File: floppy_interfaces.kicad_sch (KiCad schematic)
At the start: 23 parts, among them J13 Conn_01x04_Male, J14 Conn_02x17_Odd_Even, J16 Conn_01x04_Male, J32 Mini-DIN-8-With-Shield, J6 SDF-60J for IEC 1541 serial p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, U1 74LS373, U2 74LVC374, U22 74LS06N, U3 74LVC374, U4 74LS373

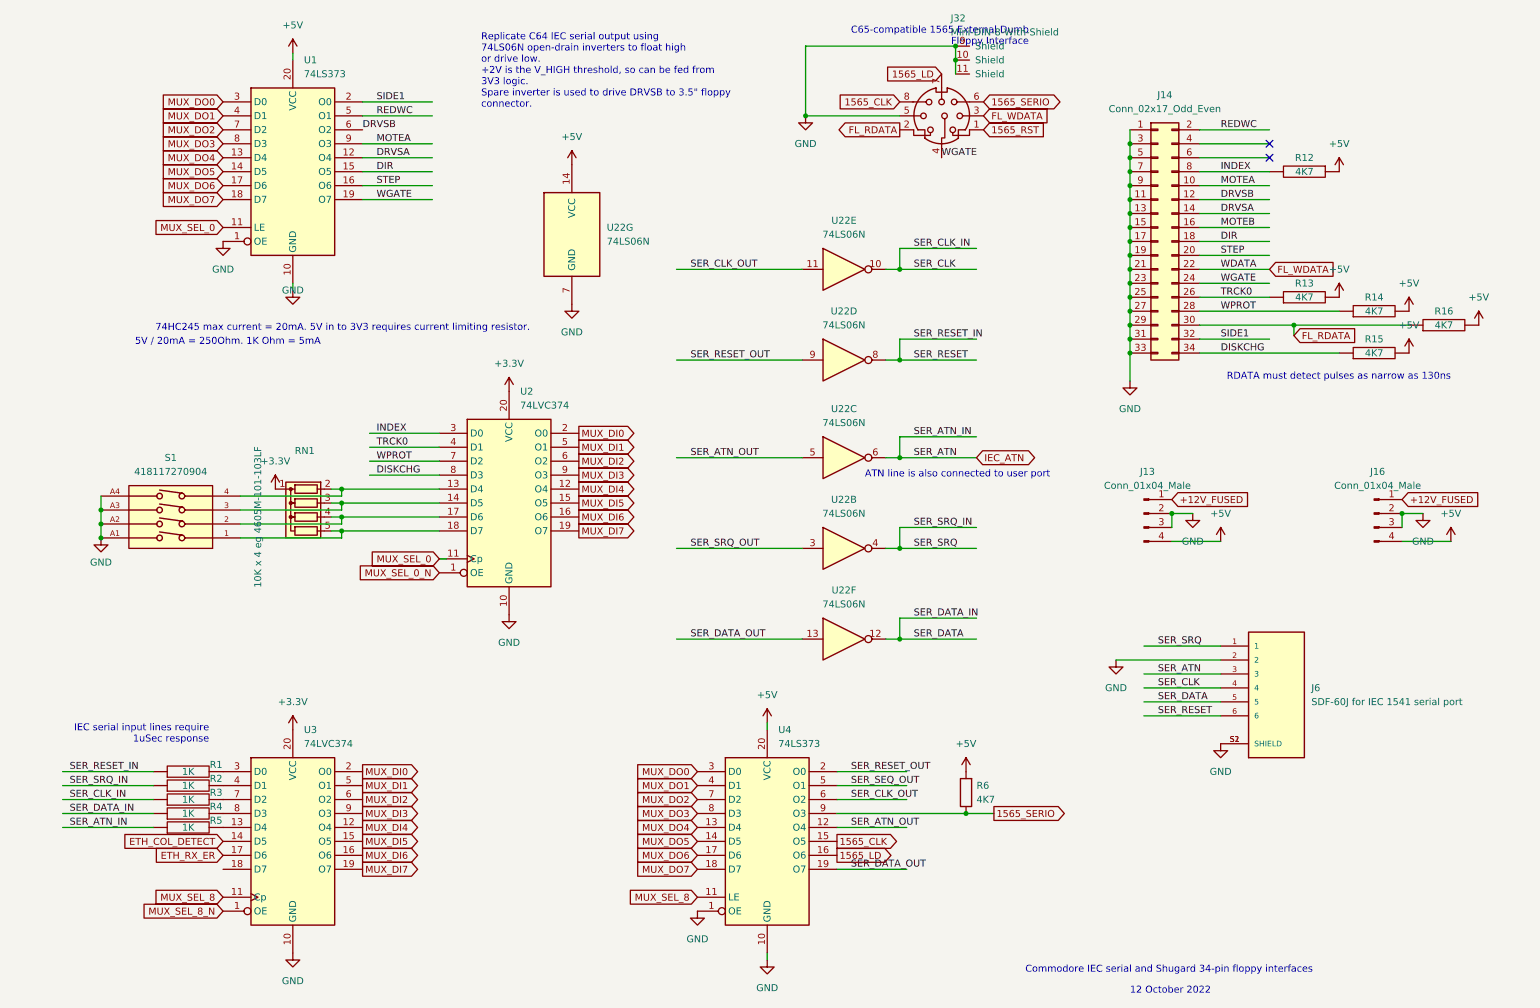
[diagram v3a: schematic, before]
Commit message: add footprints to differentiate 3.3V from 5V ICs
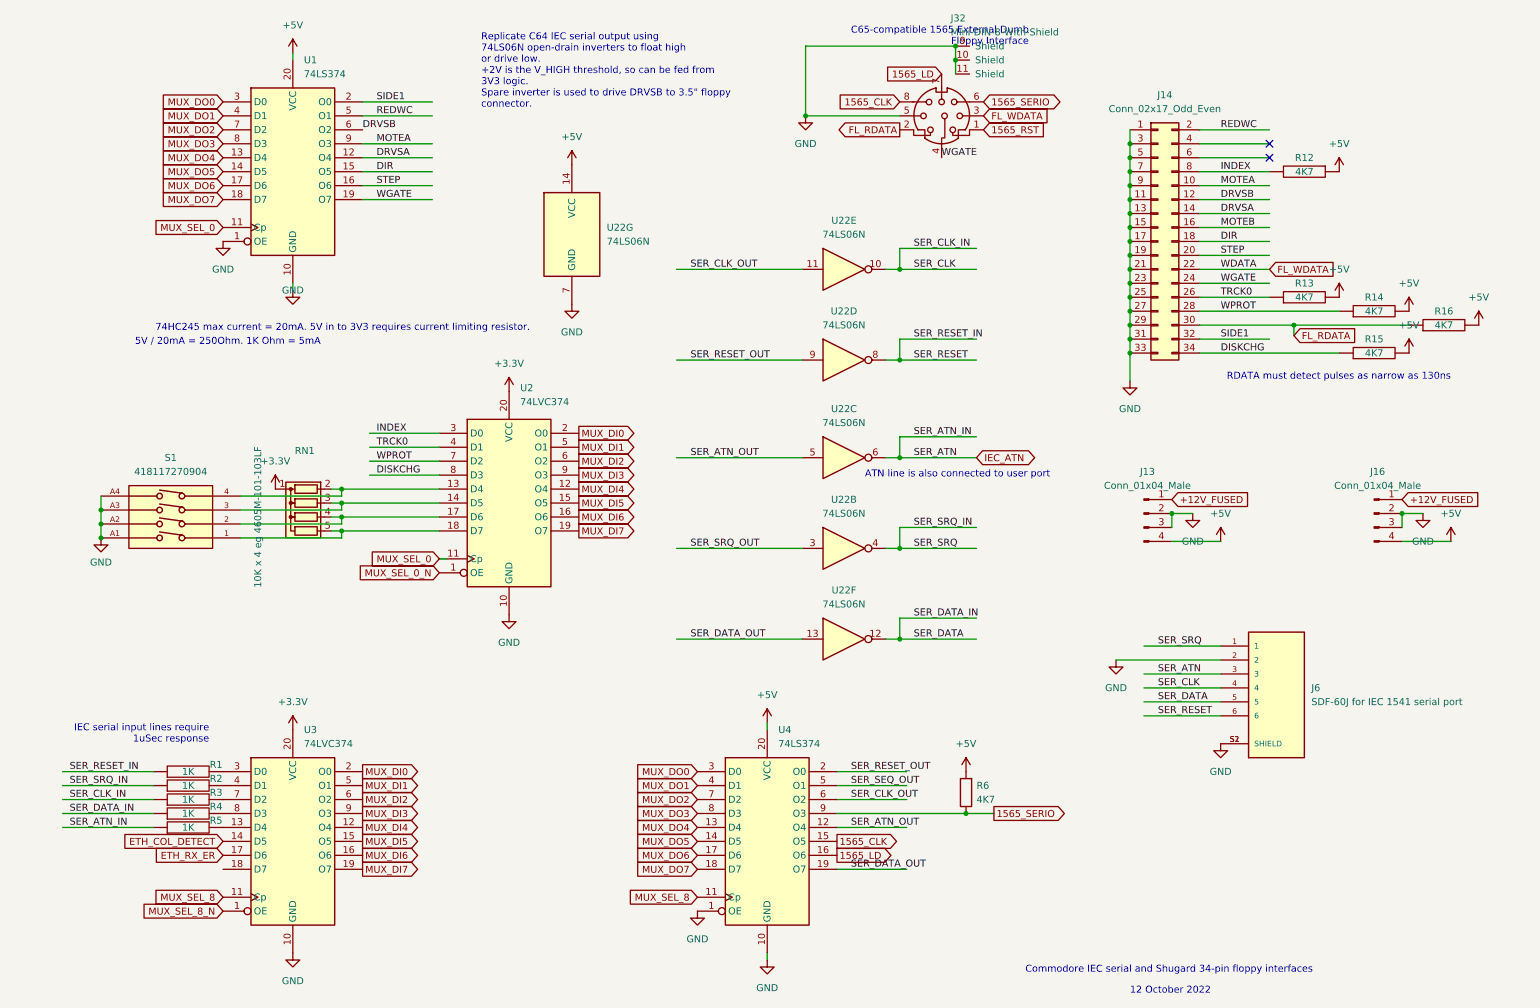
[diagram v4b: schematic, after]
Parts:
- removed U1, U4: 74LS373, Package_DIP:DIP-20_W7.62mm, symbol 74xx:74LS373
- added U1, U4: 74LS374, snapeda:DIP-20_LS_Family, symbol 74xx:74LS374
- U2, U3: footprint Package_DIP:DIP-20_W7.62mm -> snapeda:DIP-20_LVC_Family
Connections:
- net +5V: now also U1.20 (VCC), U4.20 (VCC)
- net 1565_CLK: now also U4.15 (O5)
- net 1565_LD: now also U4.16 (O6)
- net 1565_SERIO: now also U4.9 (O3)
- net DIR: now also U1.15 (O5)
- net DRVSA: now also U1.12 (O4)
- net DRVSB: now also U1.6 (O2)
- net GND: now also U1.1 (OE), U1.10 (GND), U4.1 (OE), U4.10 (GND)
- net MOTEA: now also U1.9 (O3)
- net MUX_DO0: now also U1.3 (D0), U4.3 (D0)
- net MUX_DO1: now also U1.4 (D1), U4.4 (D1)
- net MUX_DO2: now also U1.7 (D2), U4.7 (D2)
- net MUX_DO3: now also U1.8 (D3), U4.8 (D3)
- net MUX_DO4: now also U1.13 (D4), U4.13 (D4)
- net MUX_DO5: now also U1.14 (D5), U4.14 (D5)
- net MUX_DO6: now also U1.17 (D6), U4.17 (D6)
- net MUX_DO7: now also U1.18 (D7), U4.18 (D7)
- net MUX_SEL_0: now also U1.11 (Cp)
- net MUX_SEL_8: now also U4.11 (Cp)
- net REDWC: now also U1.5 (O1)
- net SER_ATN_OUT: now also U4.12 (O4)
- net SER_CLK_OUT: now also U4.6 (O2)
- net SER_DATA_OUT: now also U4.19 (O7)
- net SER_RESET_OUT: now also U4.2 (O0)
- net SER_SEQ_OUT: now also U4.5 (O1)
- net SIDE1: now also U1.2 (O0)
- net STEP: now also U1.16 (O6)
- net WGATE: now also U1.19 (O7)

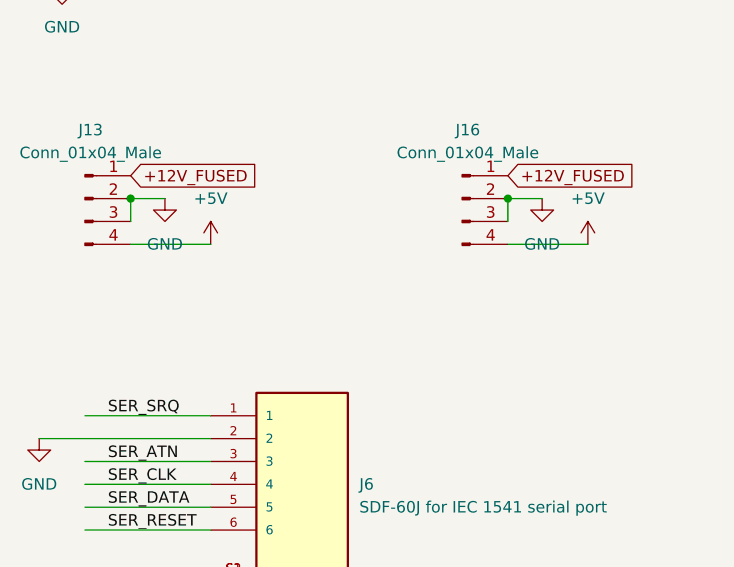
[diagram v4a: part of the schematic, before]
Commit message: fix many DRC warnings
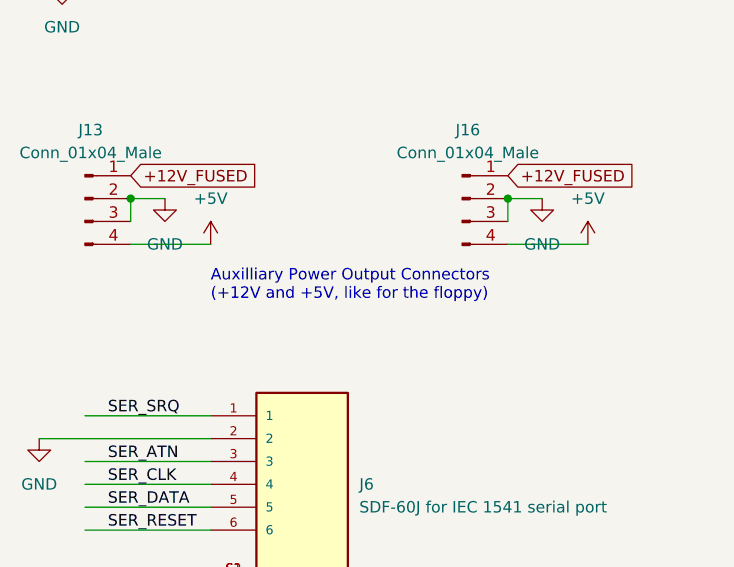
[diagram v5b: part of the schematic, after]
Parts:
- R1, R12, R13, R14, R15, R16, R2, R3, R4, R5: footprint Resistor_THT:R_Box_L8.4mm_W2.5mm_P5.08mm -> snapeda:Labeled Resistor
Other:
- note added: "Auxilliary Power Output Connectors (+12V and +5V, like for the floppy)"
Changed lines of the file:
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@@
     (effects (font (size 1.27 1.27)) (justify right bottom))
+  )
+  (text "Auxilliary Power Output Connectors\n(+12V and +5V, like for the floppy)"
+    (at 226.06 118.11 0)
+    (effects (font (size 1.27 1.27)) (justify left bottom))
   )
   (text "Replicate C64 IEC serial output using\n74LS06N open-drain inverters to float high\nor drive low.  \n+2V is the V_HIGH threshold, so can be fed from\n3V3 logic.\nSpare inverter is used to drive DRVSB to 3.5\" floppy\nconnector."
@@
     (property "Reference" "R13" (id 0) (at 241.3 64.77 90))
     (property "Value" "4K7" (id 1) (at 241.3 67.31 90))
-    (property "Footprint" "Resistor_THT:R_Box_L8.4mm_W2.5mm_P5.08mm" (id 2) (at 241.3 67.31 0)
+    (property "Footprint" "snapeda:Labeled Resistor" (id 2) (at 241.3 67.31 0)
       (effects (font (size 1.27 1.27)) hide)
     )
@@
     (property "Reference" "R2" (id 0) (at 43.18 154.94 90))
     (property "Value" "1K" (id 1) (at 38.1 156.21 90))
-    (property "Footprint" "Resistor_THT:R_Box_L8.4mm_W2.5mm_P5.08mm" (id 2) (at 38.1 156.21 0)
+    (property "Footprint" "snapeda:Labeled Resistor" (id 2) (at 38.1 156.21 0)
       (effects (font (size 1.27 1.27)) hide)
     )
@@
     (property "Reference" "R15" (id 0) (at 254 74.93 90))
     (property "Value" "4K7" (id 1) (at 254 77.47 90))
-    (property "Footprint" "Resistor_THT:R_Box_L8.4mm_W2.5mm_P5.08mm" (id 2) (at 254 77.47 0)
+    (property "Footprint" "snapeda:Labeled Resistor" (id 2) (at 254 77.47 0)
       (effects (font (size 1.27 1.27)) hide)
     )
@@
     (property "Reference" "R1" (id 0) (at 43.18 152.4 90))
     (property "Value" "1K" (id 1) (at 38.1 153.67 90))
-    (property "Footprint" "Resistor_THT:R_Box_L8.4mm_W2.5mm_P5.08mm" (id 2) (at 38.1 153.67 0)
+    (property "Footprint" "snapeda:Labeled Resistor" (id 2) (at 38.1 153.67 0)
       (effects (font (size 1.27 1.27)) hide)
     )
@@
     (property "Reference" "R5" (id 0) (at 43.18 162.56 90))
     (property "Value" "1K" (id 1) (at 38.1 163.83 90))
-    (property "Footprint" "Resistor_THT:R_Box_L8.4mm_W2.5mm_P5.08mm" (id 2) (at 38.1 163.83 0)
+    (property "Footprint" "snapeda:Labeled Resistor" (id 2) (at 38.1 163.83 0)
       (effects (font (size 1.27 1.27)) hide)
     )
@@
     (property "Reference" "R12" (id 0) (at 241.3 41.91 90))
     (property "Value" "4K7" (id 1) (at 241.3 44.45 90))
-    (property "Footprint" "Resistor_THT:R_Box_L8.4mm_W2.5mm_P5.08mm" (id 2) (at 241.3 44.45 0)
+    (property "Footprint" "snapeda:Labeled Resistor" (id 2) (at 241.3 44.45 0)
       (effects (font (size 1.27 1.27)) hide)
     )
@@
     (property "Reference" "R16" (id 0) (at 266.7 69.85 90))
     (property "Value" "4K7" (id 1) (at 266.7 72.39 90))
-    (property "Footprint" "Resistor_THT:R_Box_L8.4mm_W2.5mm_P5.08mm" (id 2) (at 266.7 72.39 0)
+    (property "Footprint" "snapeda:Labeled Resistor" (id 2) (at 266.7 72.39 0)
       (effects (font (size 1.27 1.27)) hide)
     )
@@
     (property "Reference" "R3" (id 0) (at 43.18 157.48 90))
     (property "Value" "1K" (id 1) (at 38.1 158.75 90))
-    (property "Footprint" "Resistor_THT:R_Box_L8.4mm_W2.5mm_P5.08mm" (id 2) (at 38.1 158.75 0)
+    (property "Footprint" "snapeda:Labeled Resistor" (id 2) (at 38.1 158.75 0)
       (effects (font (size 1.27 1.27)) hide)
     )
@@
     (property "Reference" "R14" (id 0) (at 254 67.31 90))
     (property "Value" "4K7" (id 1) (at 254 69.85 90))
-    (property "Footprint" "Resistor_THT:R_Box_L8.4mm_W2.5mm_P5.08mm" (id 2) (at 254 69.85 0)
+    (property "Footprint" "snapeda:Labeled Resistor" (id 2) (at 254 69.85 0)
       (effects (font (size 1.27 1.27)) hide)
     )
@@
     (property "Reference" "R4" (id 0) (at 43.18 160.02 90))
     (property "Value" "1K" (id 1) (at 38.1 161.29 90))
-    (property "Footprint" "Resistor_THT:R_Box_L8.4mm_W2.5mm_P5.08mm" (id 2) (at 38.1 161.29 0)
-      (effects (font (size 1.27 1.27)) hide)
-    )
+    (property "Footprint" "snapeda:Labeled Resistor" (id 2) (at 38.1 161.29 0)
+      (effects (font (size 1.27 1.27)) hide)
+    )

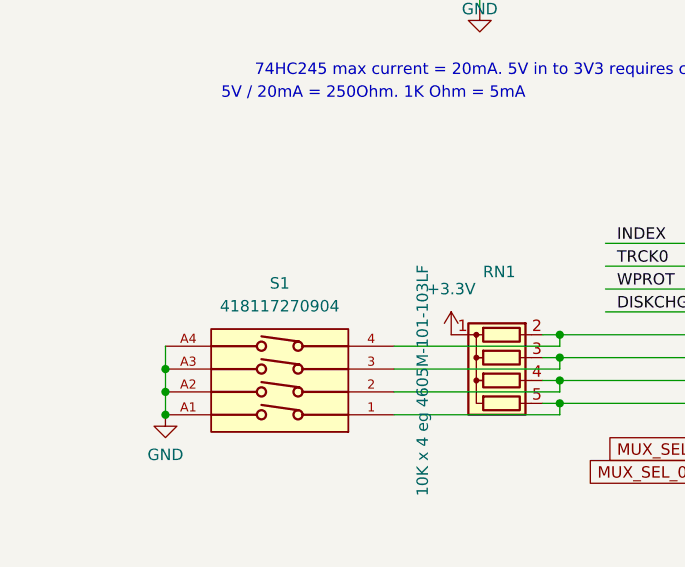
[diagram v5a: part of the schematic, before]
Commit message: re-do many labels and DRC fixes
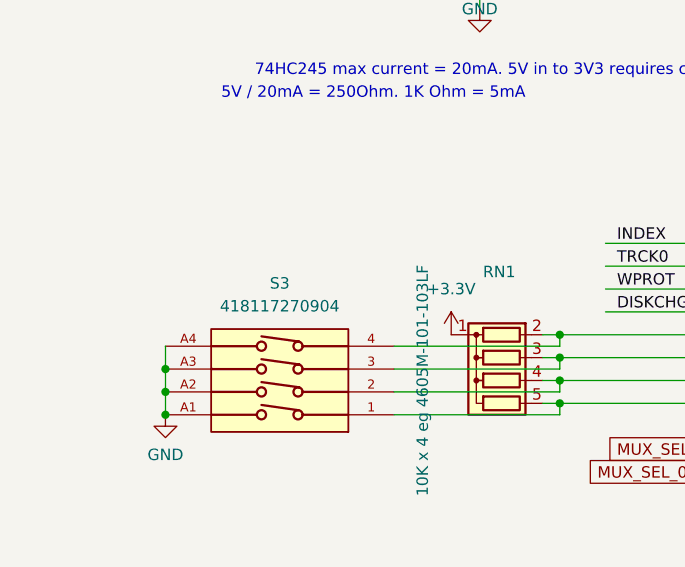
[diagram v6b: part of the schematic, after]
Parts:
- U22: footprint Package_DIP:DIP-14_W7.62mm -> snapeda:DIP-14_74LS06
- renumbered S1 to S3
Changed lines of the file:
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@@
   (symbol (lib_id "00Project-DIP-SW-4:418117270904") (at 34.925 106.045 90) (unit 1)
     (in_bom yes) (on_board yes) (fields_autoplaced)
-    (property "Reference" "S1" (id 0) (at 34.925 96.52 90))
+    (property "Reference" "S3" (id 0) (at 34.925 96.52 90))
     (property "Value" "418117270904" (id 1) (at 34.925 99.06 90))
     (property "Footprint" "418117270904" (id 2) (at 34.925 106.045 0)
@@
       (effects (font (size 1.27 1.27)) (justify left))
     )
-    (property "Footprint" "Package_DIP:DIP-14_W7.62mm" (id 2) (at 107.95 55.88 0)
+    (property "Footprint" "snapeda:DIP-14_74LS06" (id 2) (at 107.95 55.88 0)
       (effects (font (size 1.27 1.27)) hide)
     )
@@
     (property "Reference" "U22" (id 0) (at 157.48 104.14 0))
     (property "Value" "74LS06N" (id 1) (at 157.48 106.68 0))
-    (property "Footprint" "Package_DIP:DIP-14_W7.62mm" (id 2) (at 157.48 113.03 0)
+    (property "Footprint" "snapeda:DIP-14_74LS06" (id 2) (at 157.48 113.03 0)
       (effects (font (size 1.27 1.27)) hide)
     )
@@
     (property "Reference" "U22" (id 0) (at 157.48 87.63 0))
     (property "Value" "74LS06N" (id 1) (at 157.48 90.17 0))
-    (property "Footprint" "Package_DIP:DIP-14_W7.62mm" (id 2) (at 157.48 96.52 0)
+    (property "Footprint" "snapeda:DIP-14_74LS06" (id 2) (at 157.48 96.52 0)
       (effects (font (size 1.27 1.27)) hide)
     )
@@
     (property "Reference" "U22" (id 0) (at 157.48 53.34 0))
     (property "Value" "74LS06N" (id 1) (at 157.48 55.88 0))
-    (property "Footprint" "Package_DIP:DIP-14_W7.62mm" (id 2) (at 157.48 62.23 0)
+    (property "Footprint" "snapeda:DIP-14_74LS06" (id 2) (at 157.48 62.23 0)
       (effects (font (size 1.27 1.27)) hide)
     )
@@
     (property "Reference" "U22" (id 0) (at 157.48 120.65 0))
     (property "Value" "74LS06N" (id 1) (at 157.48 123.19 0))
-    (property "Footprint" "Package_DIP:DIP-14_W7.62mm" (id 2) (at 157.48 129.54 0)
+    (property "Footprint" "snapeda:DIP-14_74LS06" (id 2) (at 157.48 129.54 0)
       (effects (font (size 1.27 1.27)) hide)
     )
@@
     (property "Reference" "U22" (id 0) (at 157.48 69.85 0))
     (property "Value" "74LS06N" (id 1) (at 157.48 72.39 0))
-    (property "Footprint" "Package_DIP:DIP-14_W7.62mm" (id 2) (at 157.48 78.74 0)
-      (effects (font (size 1.27 1.27)) hide)
-    )
+    (property "Footprint" "snapeda:DIP-14_74LS06" (id 2) (at 157.48 78.74 0)
+      (effects (font (size 1.27 1.27)) hide)
+    )
